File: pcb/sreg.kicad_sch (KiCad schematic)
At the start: 1 part, among them Q1144 2N7002b

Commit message: Pi programmer.
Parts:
- renumbered Q1144 to Q981
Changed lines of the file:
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@@
   (symbol (lib_id "power:GND") (at 69.85 88.9 0)
     (in_bom yes) (on_board yes)
-    (property "Reference" "#PWR01053" (id 0) (at 69.85 95.25 0)
+    (property "Reference" "#PWR0906" (id 0) (at 69.85 95.25 0)
       (effects (font (size 1.27 1.27)) hide)
     )
@@
   (symbol (lib_id "power:GND") (at 93.98 71.12 270)
     (in_bom yes) (on_board yes)
-    (property "Reference" "#PWR01052" (id 0) (at 87.63 71.12 0)
+    (property "Reference" "#PWR0905" (id 0) (at 87.63 71.12 0)
       (effects (font (size 1.27 1.27)) hide)
     )
@@
   (symbol (lib_id "Transistor_FET:2N7002") (at 67.31 83.82 0)
     (in_bom yes) (on_board yes)
-    (property "Reference" "Q1144" (id 0) (at 72.5424 82.6516 0)
+    (property "Reference" "Q981" (id 0) (at 72.5424 82.6516 0)
       (effects (font (size 1.27 1.27)) (justify left))
     )

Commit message: Fixes
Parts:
- renumbered Q981 to Q979
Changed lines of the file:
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@@
   (symbol (lib_id "power:GND") (at 69.85 88.9 0)
     (in_bom yes) (on_board yes)
-    (property "Reference" "#PWR0906" (id 0) (at 69.85 95.25 0)
+    (property "Reference" "#PWR0902" (id 0) (at 69.85 95.25 0)
       (effects (font (size 1.27 1.27)) hide)
     )
@@
   (symbol (lib_id "power:GND") (at 93.98 71.12 270)
     (in_bom yes) (on_board yes)
-    (property "Reference" "#PWR0905" (id 0) (at 87.63 71.12 0)
+    (property "Reference" "#PWR0901" (id 0) (at 87.63 71.12 0)
       (effects (font (size 1.27 1.27)) hide)
     )
@@
   (symbol (lib_id "Transistor_FET:2N7002") (at 67.31 83.82 0)
     (in_bom yes) (on_board yes)
-    (property "Reference" "Q981" (id 0) (at 72.5424 82.6516 0)
+    (property "Reference" "Q979" (id 0) (at 72.5424 82.6516 0)
       (effects (font (size 1.27 1.27)) (justify left))
     )

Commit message: Cleanups.
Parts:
- renumbered Q979 to Q978
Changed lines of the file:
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@@
   (symbol (lib_id "power:GND") (at 69.85 88.9 0)
     (in_bom yes) (on_board yes)
-    (property "Reference" "#PWR0902" (id 0) (at 69.85 95.25 0)
+    (property "Reference" "#PWR0898" (id 0) (at 69.85 95.25 0)
       (effects (font (size 1.27 1.27)) hide)
     )
@@
   (symbol (lib_id "power:GND") (at 93.98 71.12 270)
     (in_bom yes) (on_board yes)
-    (property "Reference" "#PWR0901" (id 0) (at 87.63 71.12 0)
+    (property "Reference" "#PWR0897" (id 0) (at 87.63 71.12 0)
       (effects (font (size 1.27 1.27)) hide)
     )
@@
   (symbol (lib_id "Transistor_FET:2N7002") (at 67.31 83.82 0)
     (in_bom yes) (on_board yes)
-    (property "Reference" "Q979" (id 0) (at 72.5424 82.6516 0)
+    (property "Reference" "Q978" (id 0) (at 72.5424 82.6516 0)
       (effects (font (size 1.27 1.27)) (justify left))
     )

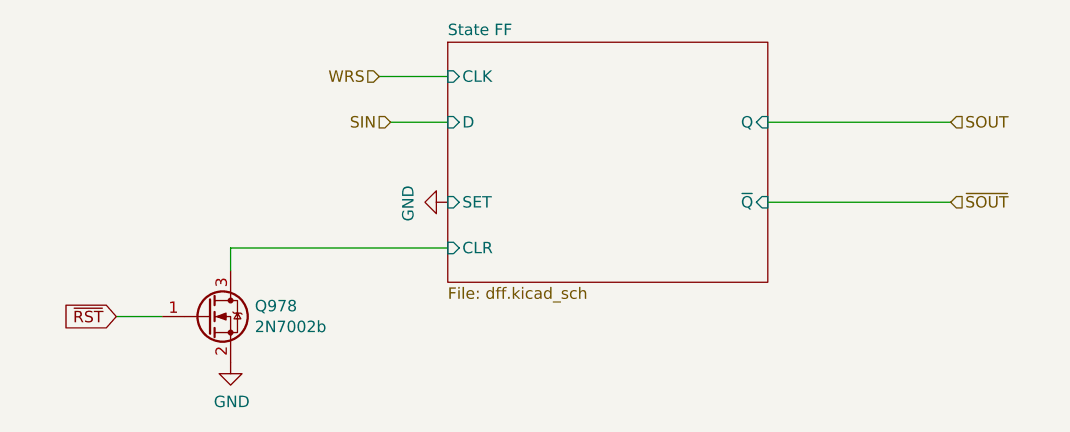
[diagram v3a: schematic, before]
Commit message: Fix UUIDs.
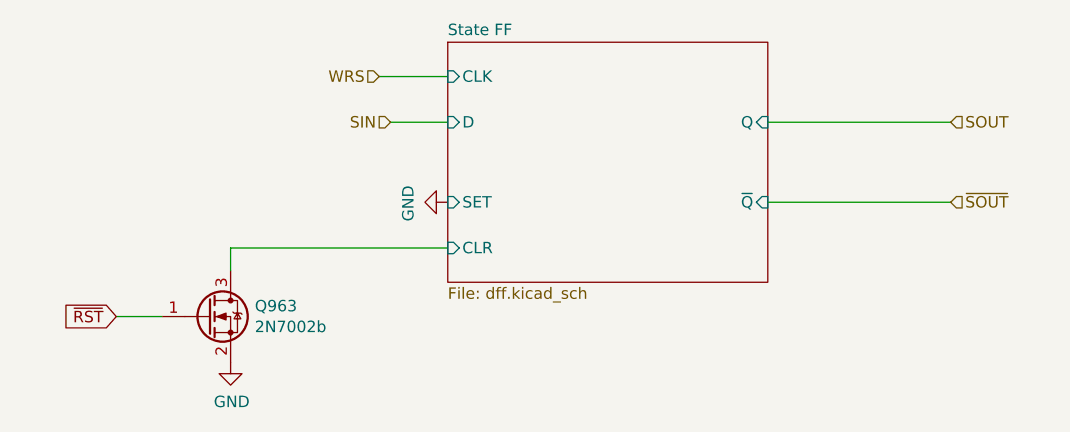
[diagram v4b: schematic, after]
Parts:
- renumbered Q978 to Q963
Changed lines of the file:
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@@
   (symbol (lib_id "power:GND") (at 69.85 88.9 0)
     (in_bom yes) (on_board yes)
-    (property "Reference" "#PWR0898" (id 0) (at 69.85 95.25 0)
+    (property "Reference" "#PWR0874" (id 0) (at 69.85 95.25 0)
       (effects (font (size 1.27 1.27)) hide)
     )
@@
   (symbol (lib_id "power:GND") (at 93.98 71.12 270)
     (in_bom yes) (on_board yes)
-    (property "Reference" "#PWR0897" (id 0) (at 87.63 71.12 0)
+    (property "Reference" "#PWR0873" (id 0) (at 87.63 71.12 0)
       (effects (font (size 1.27 1.27)) hide)
     )
@@
   (symbol (lib_id "Transistor_FET:2N7002") (at 67.31 83.82 0)
     (in_bom yes) (on_board yes)
-    (property "Reference" "Q978" (id 0) (at 72.5424 82.6516 0)
+    (property "Reference" "Q963" (id 0) (at 72.5424 82.6516 0)
       (effects (font (size 1.27 1.27)) (justify left))
     )

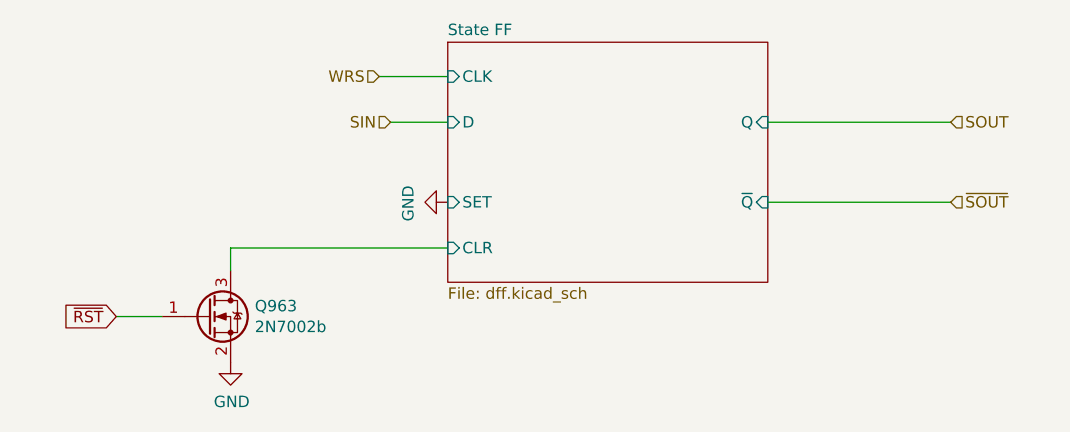
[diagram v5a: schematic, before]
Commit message: Skip ALU state for jfc/jmp/sta.
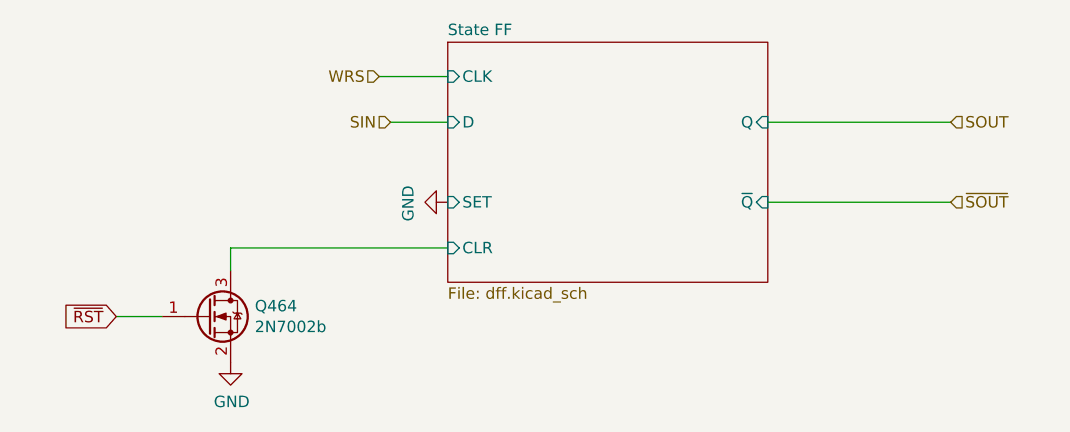
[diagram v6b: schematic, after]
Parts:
- renumbered Q963 to Q464
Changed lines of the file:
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@@
   (symbol (lib_id "Transistor_FET:2N7002") (at 67.31 83.82 0)
     (in_bom yes) (on_board yes)
-    (property "Reference" "Q963" (id 0) (at 72.5424 82.6516 0)
+    (property "Reference" "Q464" (id 0) (at 72.5424 82.6516 0)
       (effects (font (size 1.27 1.27)) (justify left))
     )

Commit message: Cleanups.
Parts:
- renumbered Q464 to Q963
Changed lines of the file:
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@@
   (symbol (lib_id "Transistor_FET:2N7002") (at 67.31 83.82 0)
     (in_bom yes) (on_board yes)
-    (property "Reference" "Q464" (id 0) (at 72.5424 82.6516 0)
+    (property "Reference" "Q963" (id 0) (at 72.5424 82.6516 0)
       (effects (font (size 1.27 1.27)) (justify left))
     )

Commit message: Some fixes.
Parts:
- removed Q963: 2N7002b, Package_TO_SOT_SMD:SOT-23, symbol Transistor_FET:2N7002
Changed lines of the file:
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@@
     (company "joewing.net")
-  )
-  (wire (pts (xy 57.15 83.82) (xy 62.23 83.82))
-    (stroke (width 0) (type solid) (color 0 0 0 0))
-  )
-  (wire (pts (xy 69.85 76.2) (xy 69.85 78.74))
-    (stroke (width 0) (type solid) (color 0 0 0 0))
-  )
-  (wire (pts (xy 69.85 76.2) (xy 93.98 76.2))
-    (stroke (width 0) (type solid) (color 0 0 0 0))
   )
   (wire (pts (xy 86.36 57.15) (xy 93.98 57.15))
@@
   )
   (wire (pts (xy 87.63 62.23) (xy 93.98 62.23))
+    (stroke (width 0) (type solid) (color 0 0 0 0))
+  )
+  (wire (pts (xy 90.17 76.2) (xy 93.98 76.2))
     (stroke (width 0) (type solid) (color 0 0 0 0))
   )
@@
     (stroke (width 0) (type solid) (color 0 0 0 0))
   )
-  (global_label "~RST" (shape input) (at 57.15 83.82 180)
-    (effects (font (size 1.27 1.27)) (justify right))
-    (property "Intersheet References" "${INTERSHEET_REFS}" (id 0) (at 0 0 0)
-      (effects (font (size 1.27 1.27)) hide)
-    )
-  )
   (hierarchical_label "WRS" (shape input) (at 86.36 57.15 180)
     (effects (font (size 1.27 1.27)) (justify right))
   )
   (hierarchical_label "SIN" (shape input) (at 87.63 62.23 180)
+    (effects (font (size 1.27 1.27)) (justify right))
+  )
+  (hierarchical_label "CLR" (shape input) (at 90.17 76.2 180)
     (effects (font (size 1.27 1.27)) (justify right))
   )
@@
     (effects (font (size 1.27 1.27)) (justify left))
   )
-  (symbol (lib_id "power:GND") (at 69.85 88.9 0)
-    (in_bom yes) (on_board yes)
-    (property "Reference" "#PWR0873" (id 0) (at 69.85 95.25 0)
-      (effects (font (size 1.27 1.27)) hide)
-    )
-    (property "Value" "GND" (id 1) (at 69.977 93.2942 0))
-    (property "Footprint" "" (id 2) (at 69.85 88.9 0)
-      (effects (font (size 1.27 1.27)) hide)
-    )
-    (property "Datasheet" "" (id 3) (at 69.85 88.9 0)
-      (effects (font (size 1.27 1.27)) hide)
-    )
-    (pin "1")
-  )
   (symbol (lib_id "power:GND") (at 93.98 71.12 270)
     (in_bom yes) (on_board yes)
-    (property "Reference" "#PWR0872" (id 0) (at 87.63 71.12 0)
+    (property "Reference" "#PWR0883" (id 0) (at 87.63 71.12 0)
       (effects (font (size 1.27 1.27)) hide)
     )
@@
     (pin "1")
   )
-  (symbol (lib_id "Transistor_FET:2N7002") (at 67.31 83.82 0)
-    (in_bom yes) (on_board yes)
-    (property "Reference" "Q963" (id 0) (at 72.5424 82.6516 0)
-      (effects (font (size 1.27 1.27)) (justify left))
-    )
-    (property "Value" "2N7002b" (id 1) (at 72.542 84.963 0)
-      (effects (font (size 1.27 1.27)) (justify left))
-    )
-    (property "Footprint" "Package_TO_SOT_SMD:SOT-23" (id 2) (at 72.39 85.725 0)
-      (effects (font (size 1.27 1.27) italic) (justify left) hide)
-    )
-    (property "Datasheet" "https://www.fairchildsemi.com/datasheets/2N/2N7002.pdf" (id 3) (at 67.31 83.82 0)
-      (effects (font (size 1.27 1.27)) (justify left) hide)
-    )
-    (property "LCSC" "C8545" (id 4) (at 67.31 83.82 0)
-      (effects (font (size 1.27 1.27)) hide)
-    )
-    (pin "1")
-    (pin "2")
-    (pin "3")
-  )
   (sheet (at 93.98 53.34) (size 35.56 26.67)
